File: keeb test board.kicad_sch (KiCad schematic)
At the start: 17 parts, among them SW12 SW_Push, SW14 SW_Push, SW15 SW_Push, SW3 SW_Push, SW6 SW_Push, SW9 SW_Push, U1 BluePill_V1.1

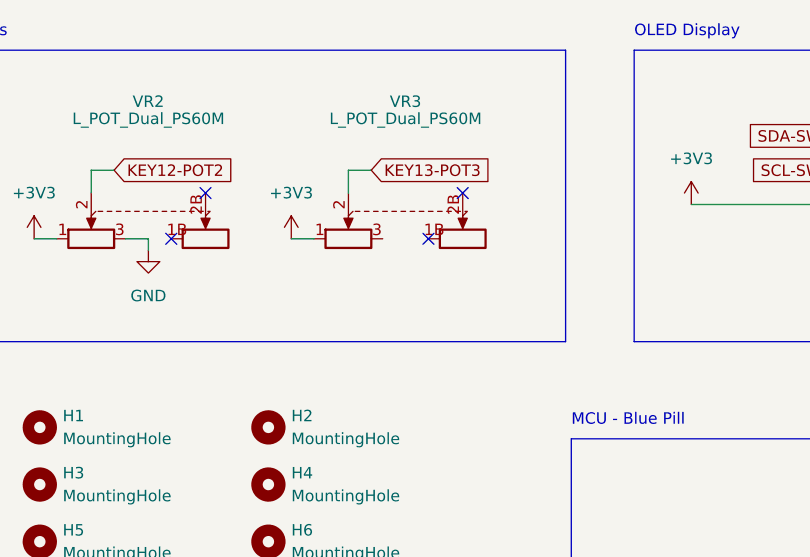
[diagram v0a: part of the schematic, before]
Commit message: updated libs, positioned jumpers
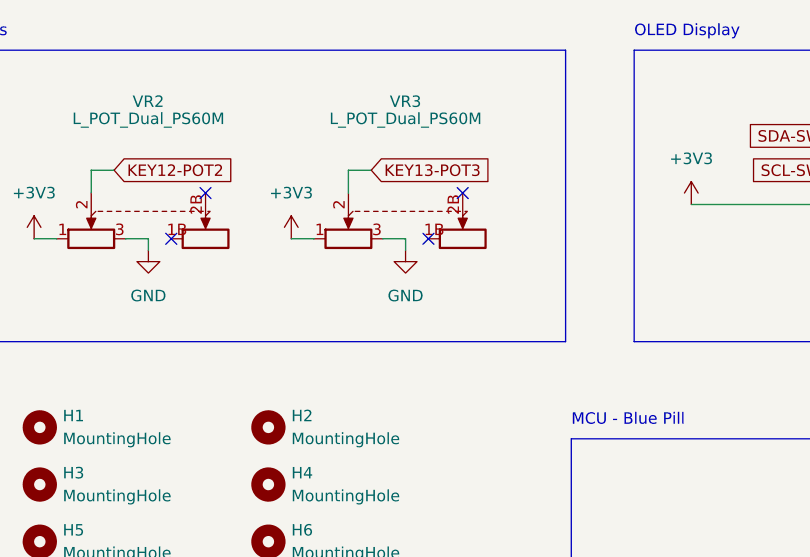
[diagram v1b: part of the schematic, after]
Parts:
- U1: symbol YAAJ_BluePill:YAAJ_BluePill_BHTS -> YAAJ_BluePill_modified:YAAJ_BluePill_BHTS
- VR1, VR2, VR3: symbol deej_PS60:L_POT_Dual_PS60M_combo -> PS60 Linear Potentiometer:L_POT_Dual_PS60M_combo
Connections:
- net GND: now also VR3.3
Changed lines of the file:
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@@
     (stroke (width 0) (type solid) (color 0 194 0 1))
+  )
+  (wire (pts (xy 151.13 43.815) (xy 151.13 45.085))
+    (stroke (width 0) (type default) (color 0 0 0 0))
   )
   (wire (pts (xy 190.5 106.68) (xy 191.77 106.68))
@@
   )
   (polyline (pts (xy 74.93 22.86) (xy 168.91 22.86))
+    (stroke (width 0) (type default) (color 0 0 0 0))
+  )
+  (wire (pts (xy 148.59 43.815) (xy 151.13 43.815))
     (stroke (width 0) (type default) (color 0 0 0 0))
   )
@@
     (pin "2")
   )
-  (symbol (lib_id "deej_PS60:L_POT_Dual_PS60M_combo") (at 92.075 40.64 0) (unit 1)
+  (symbol (lib_id "PS60 Linear Potentiometer:L_POT_Dual_PS60M_combo") (at 92.075 40.64 0) (unit 1)
     (in_bom yes) (on_board yes)
     (property "Reference" "VR1" (id 0) (at 92.075 27.94 0))
@@
     (pin "3")
   )
-  (symbol (lib_id "YAAJ_BluePill:YAAJ_BluePill_BHTS") (at 212.09 111.76 0) (unit 1)
+  (symbol (lib_id "YAAJ_BluePill_modified:YAAJ_BluePill_BHTS") (at 212.09 111.76 0) (unit 1)
     (in_bom yes) (on_board yes) (fields_autoplaced)
     (property "Reference" "U1" (id 0) (at 198.12 87.63 0))
@@
     (pin "1")
   )
-  (symbol (lib_id "deej_PS60:L_POT_Dual_PS60M_combo") (at 151.13 41.275 0) (unit 1)
+  (symbol (lib_id "PS60 Linear Potentiometer:L_POT_Dual_PS60M_combo") (at 151.13 41.275 0) (unit 1)
     (in_bom yes) (on_board yes)
     (property "Reference" "VR3" (id 0) (at 151.13 28.575 0))
@@
     (pin "1")
   )
-  (symbol (lib_id "deej_PS60:L_POT_Dual_PS60M_combo") (at 122.555 41.275 0) (unit 1)
+  (symbol (lib_id "PS60 Linear Potentiometer:L_POT_Dual_PS60M_combo") (at 122.555 41.275 0) (unit 1)
     (in_bom yes) (on_board yes)
     (property "Reference" "VR2" (id 0) (at 122.555 28.575 0))
@@
     )
     (property "Datasheet" "" (id 3) (at 95.885 99.06 0)
+      (effects (font (size 1.27 1.27)) hide)
+    )
+    (pin "1")
+  )
+  (symbol (lib_id "power:GND") (at 151.13 45.085 0) (unit 1)
+    (in_bom yes) (on_board yes) (fields_autoplaced)
+    (property "Reference" "#PWR0118" (id 0) (at 151.13 51.435 0)
+      (effects (font (size 1.27 1.27)) hide)
+    )
+    (property "Value" "GND" (id 1) (at 151.13 50.165 0))
+    (property "Footprint" "" (id 2) (at 151.13 45.085 0)
+      (effects (font (size 1.27 1.27)) hide)
+    )
+    (property "Datasheet" "" (id 3) (at 151.13 45.085 0)
       (effects (font (size 1.27 1.27)) hide)
     )
@@
       (reference "#PWR0117") (unit 1) (value "GND") (footprint "")
     )
+    (path "/9e7c36da-71f2-4ced-bdff-20b347a99063"
+      (reference "#PWR0118") (unit 1) (value "GND") (footprint "")
+    )
     (path "/6ce8230c-595b-49b4-b7e1-27c56bb79809/49cf5ed7-5634-4152-93c3-794466e8f794"
       (reference "D1") (unit 1) (value "SK6812MINI") (footprint "marbastlib-mx:LED_MX_6028R_lower-offset")
@@
     )
     (path "/6ce8230c-595b-49b4-b7e1-27c56bb79809/17d2d7d2-ca40-4a79-aad9-55b86398d62f"
-      (reference "JP5") (unit 1) (value "SolderJumper_2_Open") (footprint "Keeby-Cat Footprints:SolderJumper-2_P1.3mm_Open_TrianglePad1.0x1.5mm")
+      (reference "JP9") (unit 1) (value "SolderJumper_2_Open") (footprint "Keeby-Cat Footprints:SolderJumper-2_P1.3mm_Open_TrianglePad1.0x1.5mm")
     )
     (path "/6ce8230c-595b-49b4-b7e1-27c56bb79809/a88febab-e94f-47d4-8fcb-06aae5f3019c"
-      (reference "JP6") (unit 1) (value "SolderJumper_2_Open") (footprint "Keeby-Cat Footprints:SolderJumper-2_P1.3mm_Open_TrianglePad1.0x1.5mm")
+      (reference "JP10") (unit 1) (value "SolderJumper_2_Open") (footprint "Keeby-Cat Footprints:SolderJumper-2_P1.3mm_Open_TrianglePad1.0x1.5mm")
     )
     (path "/6ce8230c-595b-49b4-b7e1-27c56bb79809/0fb88d47-c573-4cb7-b77a-3903da88fc3f"
-      (reference "JP7") (unit 1) (value "SolderJumper_2_Open") (footprint "Keeby-Cat Footprints:SolderJumper-2_P1.3mm_Open_TrianglePad1.0x1.5mm")
+      (reference "JP11") (unit 1) (value "SolderJumper_2_Open") (footprint "Keeby-Cat Footprints:SolderJumper-2_P1.3mm_Open_TrianglePad1.0x1.5mm")
     )
     (path "/6ce8230c-595b-49b4-b7e1-27c56bb79809/409a2743-ade4-4007-b114-b5278d2cd8cd"
-      (reference "JP8") (unit 1) (value "SolderJumper_2_Open") (footprint "Keeby-Cat Footprints:SolderJumper-2_P1.3mm_Open_TrianglePad1.0x1.5mm")
+      (reference "JP12") (unit 1) (value "SolderJumper_2_Open") (footprint "Keeby-Cat Footprints:SolderJumper-2_P1.3mm_Open_TrianglePad1.0x1.5mm")
     )
     (path "/6ce8230c-595b-49b4-b7e1-27c56bb79809/12ccb95a-3131-4207-beec-6198c34fd72e"
-      (reference "JP9") (unit 1) (value "SolderJumper_2_Open") (footprint "Keeby-Cat Footprints:SolderJumper-2_P1.3mm_Open_TrianglePad1.0x1.5mm")
+      (reference "JP13") (unit 1) (value "SolderJumper_2_Open") (footprint "Keeby-Cat Footprints:SolderJumper-2_P1.3mm_Open_TrianglePad1.0x1.5mm")
     )
     (path "/6ce8230c-595b-49b4-b7e1-27c56bb79809/cd64c52e-128a-4186-ac52-c59b781981b9"

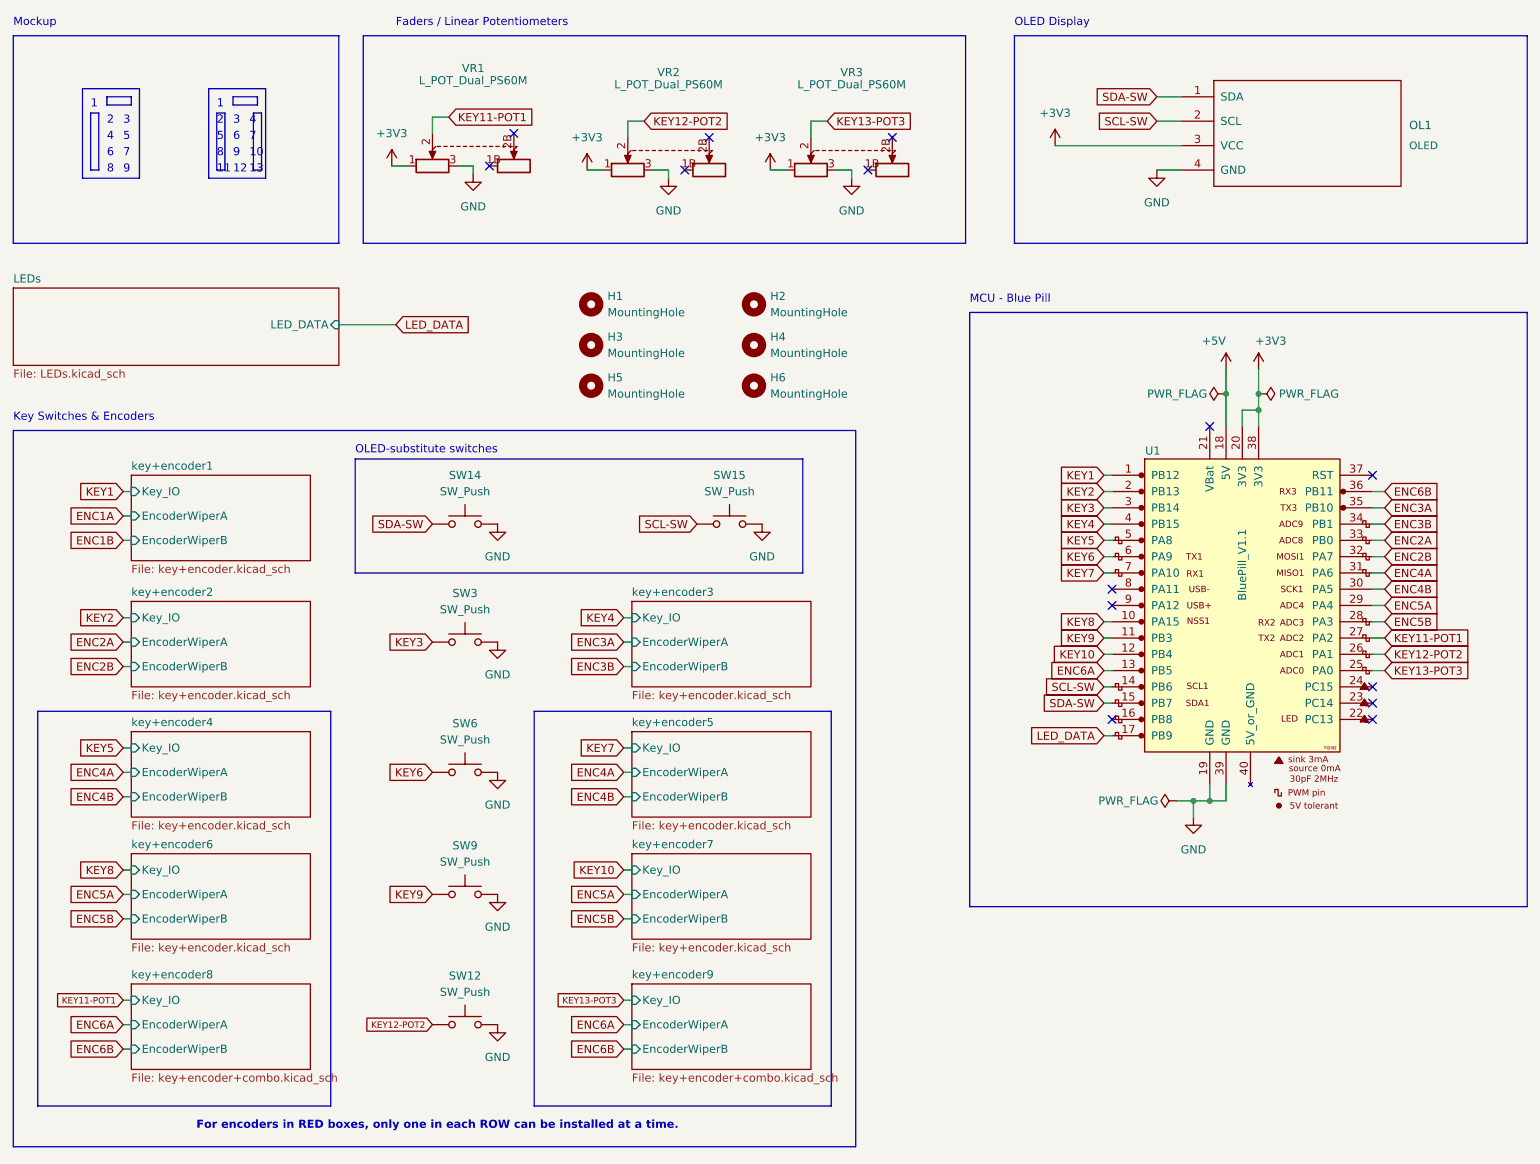
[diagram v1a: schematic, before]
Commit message: initial board routing
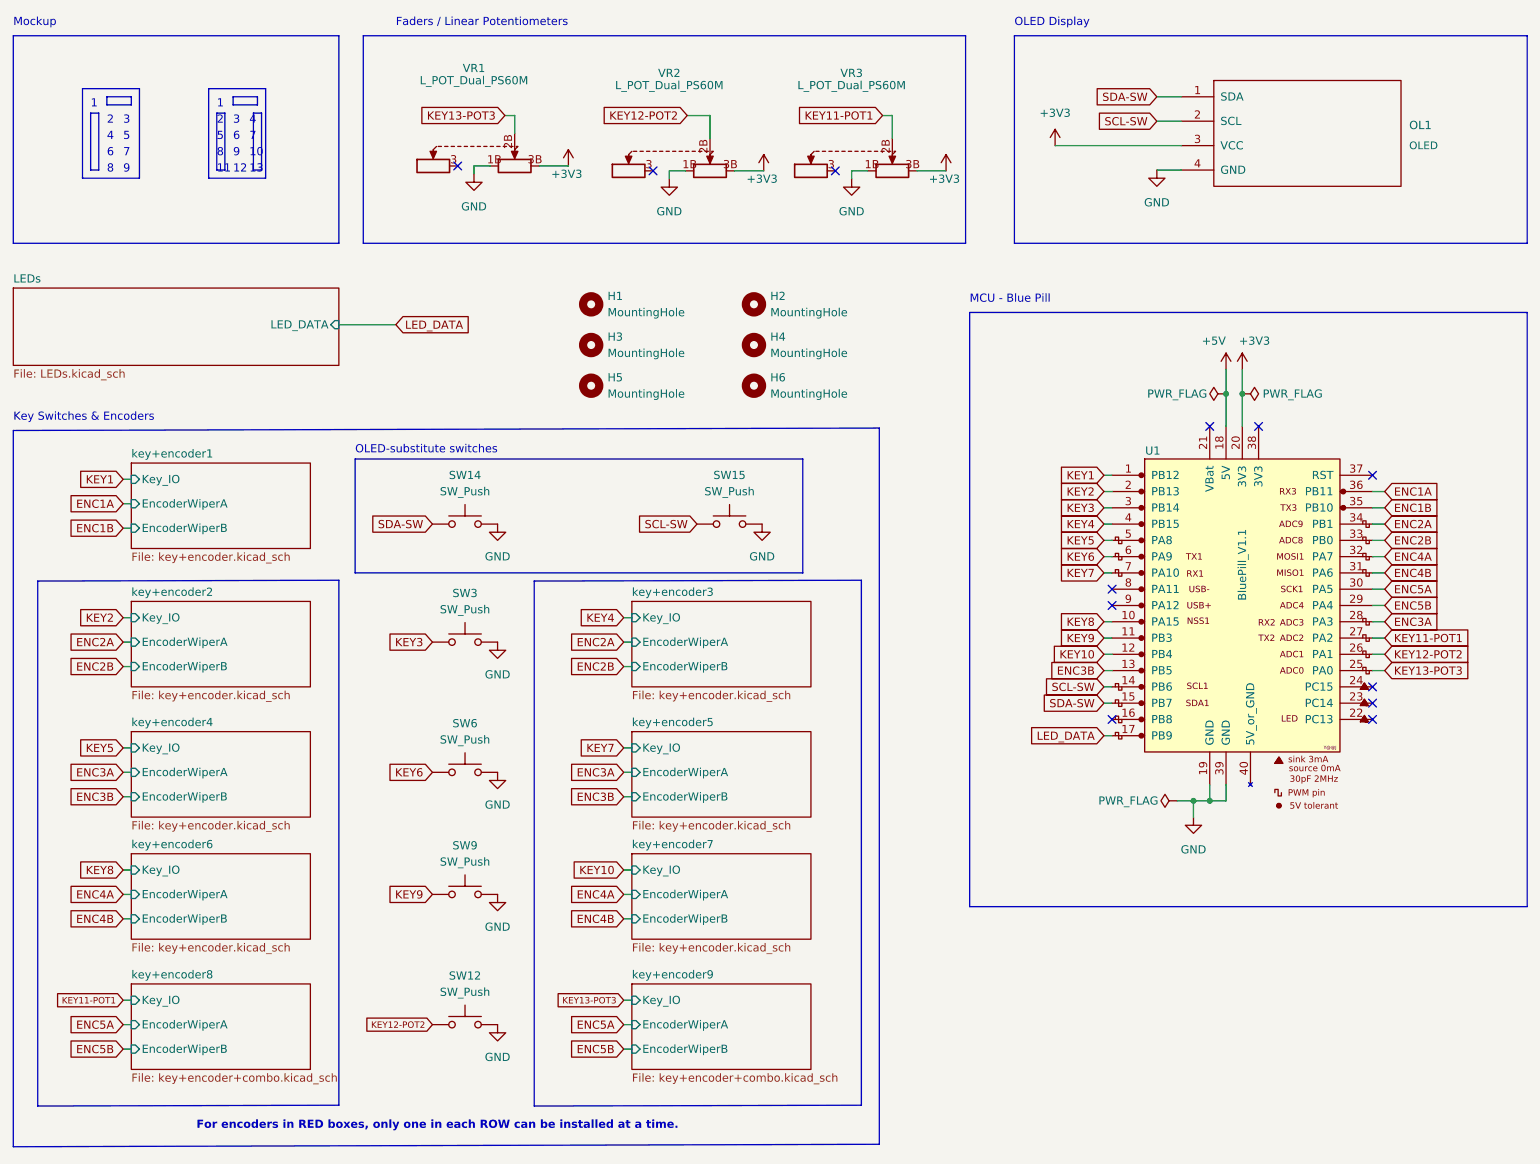
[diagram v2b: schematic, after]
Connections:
- net ENC6A is gone; now on net ENC3B: U1.13 (PB5)
- net ENC6B is gone; now on net ENC1A: U1.36 (PB11)
- net +3V3: now also VR1.3B, VR2.3B, VR3.3B; no longer U1.38 (3V3), VR1.1, VR2.1, VR3.1
- net ENC1B: now also U1.35 (PB10)
- net ENC2A: now also U1.34 (PB1); no longer U1.33 (PB0)
- net ENC2B: now also U1.33 (PB0); no longer U1.32 (PA7)
- net ENC3A: now also U1.28 (PA3); no longer U1.35 (PB10)
- net ENC3B: no longer U1.34 (PB1)
- net ENC4A: now also U1.32 (PA7); no longer U1.31 (PA6)
- net ENC4B: now also U1.31 (PA6); no longer U1.30 (PA5)
- net ENC5A: now also U1.30 (PA5); no longer U1.29 (PA4)
- net ENC5B: now also U1.29 (PA4); no longer U1.28 (PA3)
- net GND: now also VR1.1B, VR2.1B, VR3.1B; no longer VR1.3, VR2.3, VR3.3
- net KEY11-POT1: now also VR3.2B; no longer VR1.2
- net KEY12-POT2: now also VR2.2B; no longer VR2.2
- net KEY13-POT3: now also VR1.2B; no longer VR3.2
- no-connect marks 14 -> 12

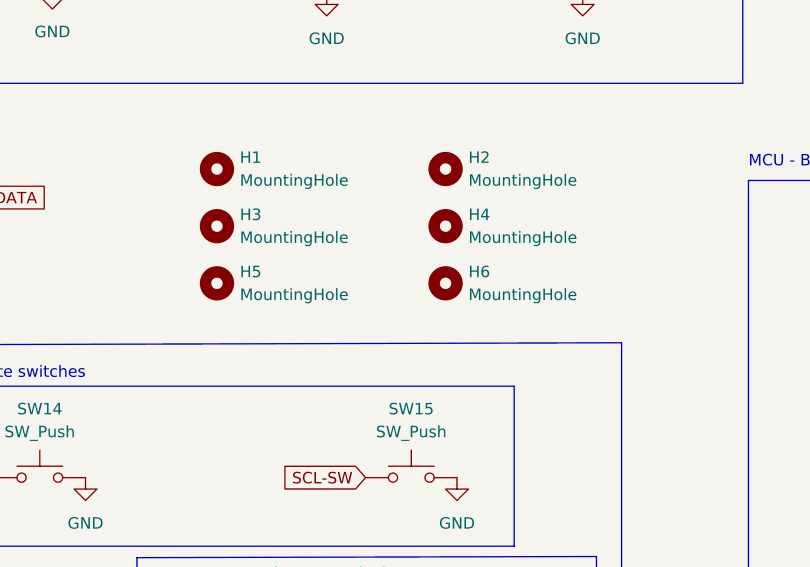
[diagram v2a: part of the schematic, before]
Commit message: shrank board outline to 100mm max
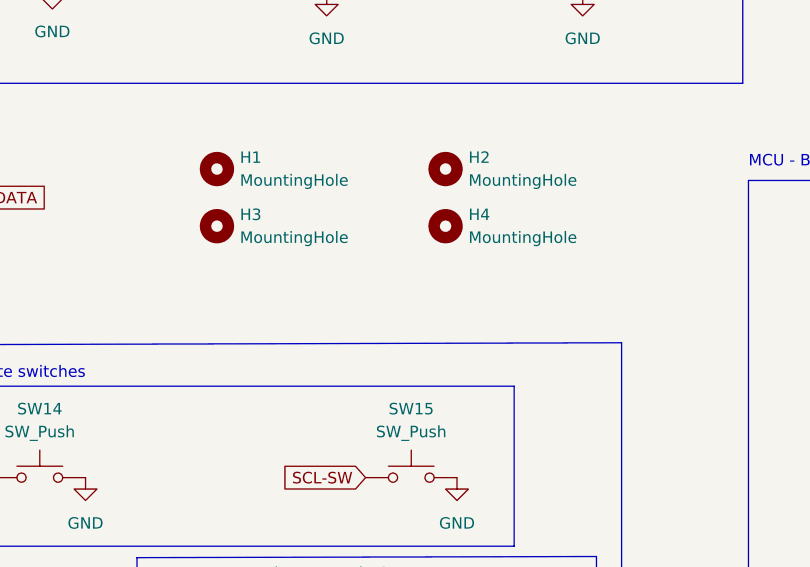
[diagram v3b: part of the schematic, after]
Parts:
- removed H5, H6: MountingHole, Keeby-Cat Footprints:MountingHole_3.2mm_M3_Half, symbol Mechanical:MountingHole
- H1, H2: footprint deej DVC-5-L prepanel:MountingHole_3.2mm_M3_Half -> MountingHole:MountingHole_2.2mm_M2_DIN965
- H3, H4: footprint MountingHole:MountingHole_3.2mm_M3 -> MountingHole:MountingHole_2.2mm_M2_DIN965
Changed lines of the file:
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@@
     (pin "3B")
-  )
-  (symbol (lib_id "Mechanical:MountingHole") (at 135.89 77.47 0) (unit 1)
-    (in_bom yes) (on_board yes) (fields_autoplaced)
-    (property "Reference" "H6" (id 0) (at 138.43 76.1999 0)
-      (effects (font (size 1.27 1.27)) (justify left))
-    )
-    (property "Value" "MountingHole" (id 1) (at 138.43 78.7399 0)
-      (effects (font (size 1.27 1.27)) (justify left))
-    )
-    (property "Footprint" "Keeby-Cat Footprints:MountingHole_3.2mm_M3_Half" (id 2) (at 135.89 77.47 0)
-      (effects (font (size 1.27 1.27)) hide)
-    )
-    (property "Datasheet" "~" (id 3) (at 135.89 77.47 0)
-      (effects (font (size 1.27 1.27)) hide)
-    )
   )
   (symbol (lib_id "Switch:SW_Push") (at 132.08 99.06 0) (unit 1)
@@
       (effects (font (size 1.27 1.27)) (justify left))
     )
-    (property "Footprint" "deej DVC-5-L prepanel:MountingHole_3.2mm_M3_Half" (id 2) (at 135.89 64.77 0)
+    (property "Footprint" "MountingHole:MountingHole_2.2mm_M2_DIN965" (id 2) (at 135.89 64.77 0)
       (effects (font (size 1.27 1.27)) hide)
     )
@@
       (effects (font (size 1.27 1.27)) (justify left))
     )
-    (property "Footprint" "MountingHole:MountingHole_3.2mm_M3" (id 2) (at 135.89 71.12 0)
+    (property "Footprint" "MountingHole:MountingHole_2.2mm_M2_DIN965" (id 2) (at 135.89 71.12 0)
       (effects (font (size 1.27 1.27)) hide)
     )
@@
     (pin "1")
   )
-  (symbol (lib_id "Mechanical:MountingHole") (at 110.49 77.47 0) (unit 1)
-    (in_bom yes) (on_board yes) (fields_autoplaced)
-    (property "Reference" "H5" (id 0) (at 113.03 76.1999 0)
-      (effects (font (size 1.27 1.27)) (justify left))
-    )
-    (property "Value" "MountingHole" (id 1) (at 113.03 78.7399 0)
-      (effects (font (size 1.27 1.27)) (justify left))
-    )
-    (property "Footprint" "Keeby-Cat Footprints:MountingHole_3.2mm_M3_Half" (id 2) (at 110.49 77.47 0)
-      (effects (font (size 1.27 1.27)) hide)
-    )
-    (property "Datasheet" "~" (id 3) (at 110.49 77.47 0)
-      (effects (font (size 1.27 1.27)) hide)
-    )
-  )
   (symbol (lib_id "Switch:SW_Push") (at 90.805 99.06 0) (unit 1)
     (in_bom yes) (on_board yes) (fields_autoplaced)
@@
       (effects (font (size 1.27 1.27)) (justify left))
     )
-    (property "Footprint" "deej DVC-5-L prepanel:MountingHole_3.2mm_M3_Half" (id 2) (at 110.49 64.77 0)
+    (property "Footprint" "MountingHole:MountingHole_2.2mm_M2_DIN965" (id 2) (at 110.49 64.77 0)
       (effects (font (size 1.27 1.27)) hide)
     )
@@
       (effects (font (size 1.27 1.27)) (justify left))
     )
-    (property "Footprint" "MountingHole:MountingHole_3.2mm_M3" (id 2) (at 110.49 71.12 0)
+    (property "Footprint" "MountingHole:MountingHole_2.2mm_M2_DIN965" (id 2) (at 110.49 71.12 0)
       (effects (font (size 1.27 1.27)) hide)
     )
@@
     )
     (path "/d7dc8332-4e7d-4d1c-9e13-94700025e229"
-      (reference "H1") (unit 1) (value "MountingHole") (footprint "deej DVC-5-L prepanel:MountingHole_3.2mm_M3_Half")
+      (reference "H1") (unit 1) (value "MountingHole") (footprint "MountingHole:MountingHole_2.2mm_M2_DIN965")
     )
     (path "/5a7e5e4b-0f2c-4c71-9d32-45cf0732b0c3"
-      (reference "H2") (unit 1) (value "MountingHole") (footprint "deej DVC-5-L prepanel:MountingHole_3.2mm_M3_Half")
+      (reference "H2") (unit 1) (value "MountingHole") (footprint "MountingHole:MountingHole_2.2mm_M2_DIN965")
     )
     (path "/f81e2caa-f7a2-40dd-8668-c447b8223c0a"
-      (reference "H3") (unit 1) (value "MountingHole") (footprint "MountingHole:MountingHole_3.2mm_M3")
+      (reference "H3") (unit 1) (value "MountingHole") (footprint "MountingHole:MountingHole_2.2mm_M2_DIN965")
     )
     (path "/8ea18563-8d92-48ab-81f4-e90c6181f6de"
-      (reference "H4") (unit 1) (value "MountingHole") (footprint "MountingHole:MountingHole_3.2mm_M3")
-    )
-    (path "/c1065595-ce0f-4f5b-9a39-98e166d74826"
-      (reference "H5") (unit 1) (value "MountingHole") (footprint "Keeby-Cat Footprints:MountingHole_3.2mm_M3_Half")
-    )
-    (path "/32772fda-346b-4fe0-8a82-8e5d42102caa"
-      (reference "H6") (unit 1) (value "MountingHole") (footprint "Keeby-Cat Footprints:MountingHole_3.2mm_M3_Half")
+      (reference "H4") (unit 1) (value "MountingHole") (footprint "MountingHole:MountingHole_2.2mm_M2_DIN965")
     )
     (path "/6ce8230c-595b-49b4-b7e1-27c56bb79809/368da0b2-4a09-4c1c-a7bd-9829d431f181"
